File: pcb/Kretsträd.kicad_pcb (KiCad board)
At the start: 2 copper layers, 112.5 x 95.1 mm, 58 parts, among them J1 Conn_01x02_Female, J2 Conn_01x02_Female, J3 Conn_01x02_Female, SW1 SW_PUSH, SW10 SW_PUSH, SW11 SW_PUSH, SW12 SW_PUSH, SW13 SW_PUSH, SW14 SW_PUSH, SW15 SW_PUSH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

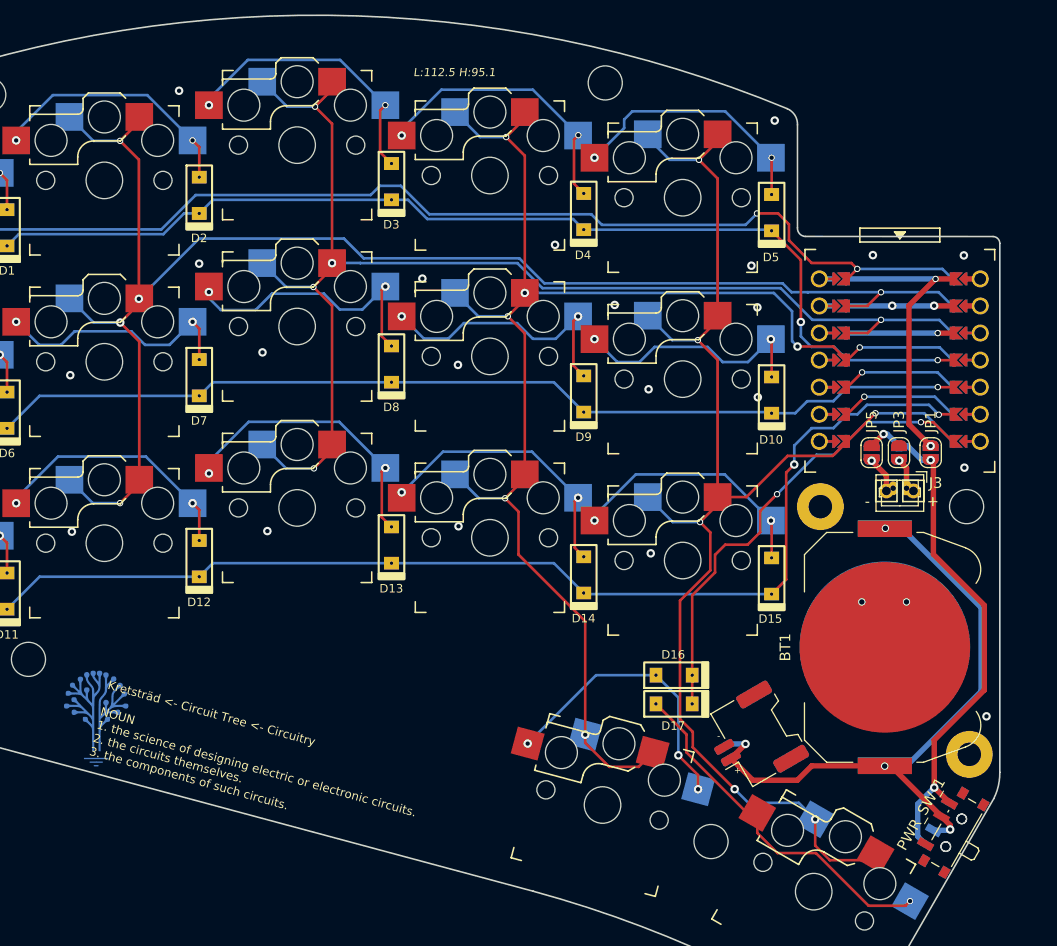
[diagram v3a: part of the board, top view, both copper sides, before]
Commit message: Moved position of CR2032 battery holder, some mounting holes.
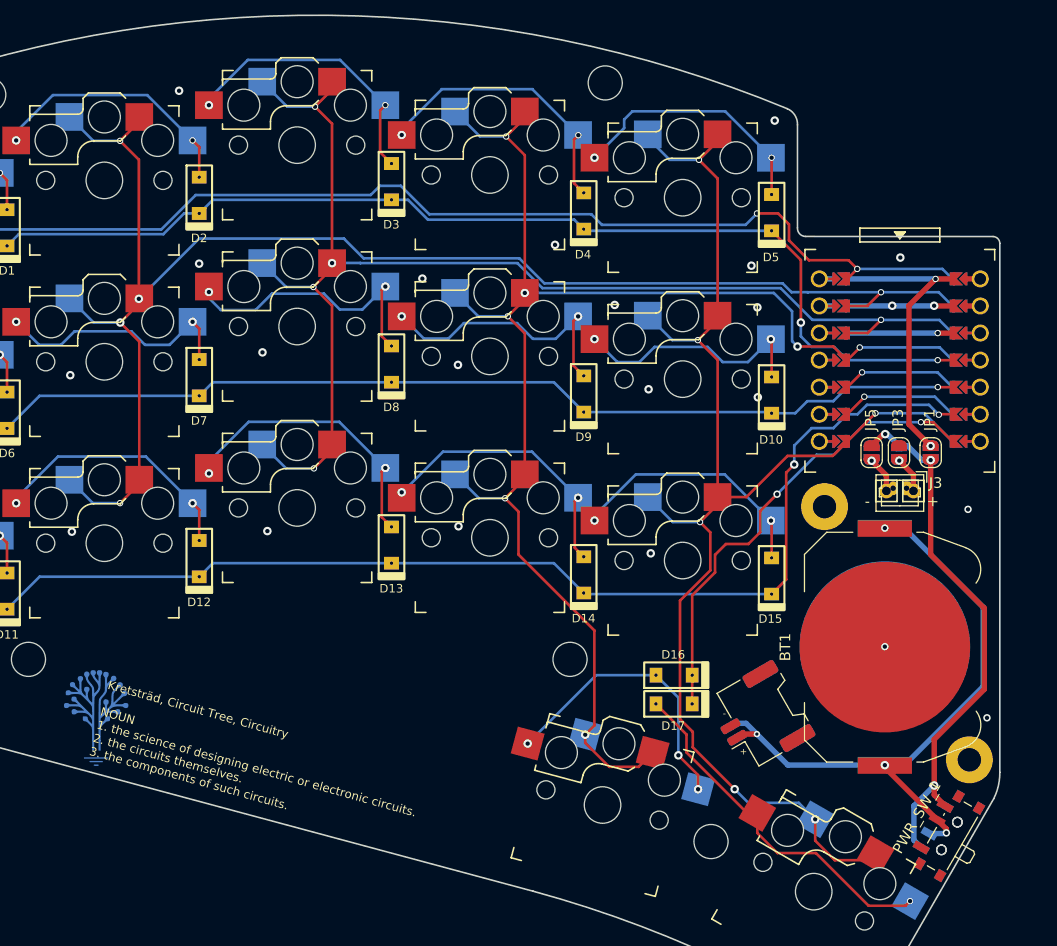
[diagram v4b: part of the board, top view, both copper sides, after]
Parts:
- moved TH5 39.9 mm to (154.6, 106.9)
- moved J1 2.02 mm to (172.4, 112.4)
- moved J2 2.02 mm to (172.4, 112.4)
- moved TH_PCB_2 0.51 mm to (192.0, 116.4)
- moved PWR_SW_1 0.51 mm to (189.9, 123.3)
- moved PWR_SW_2 0.51 mm to (189.9, 123.3)
- moved TH_PCB_1 0.39 mm to (178.4, 92.6)
- moved D4 0.05 mm to (155.9, 64.9)
- moved SW4 0.05 mm to (147.0, 61.5)
- moved G*** 0.05 mm to (109.9, 111.4)
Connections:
- SW1 pad : col0 -> (no net)
- SW11 pad : col0 -> (no net)
- SW6 pad : col0 -> (no net)
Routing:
- net BT+: track 62.4 -> 55.8 mm
- net col4: track 127.4 -> 126.4 mm
- net col3: track 134.7 -> 135.4 mm
- net row0: track 101.4 -> 100.7 mm
- net Net-(JP1-Pad1): track 50.1 -> 50.8 mm
- net Hole_1: track 2.87 -> 3.40 mm
- net GND: track 9.88 -> 9.87 mm, vias 26 -> 24
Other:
- board text added: "Kretsträd, Circuit Tree, Circuitry NOUN 1. the science of designing electric or electronic circuits. 2. the circuits themselves. 3. the components of such circuits."
- board text removed: "Kretsträd <- Circuit Tree <- Circuitry NOUN 1. the science of designing electric or electronic circuits. 2. the circuits themselves. 3. the components of such circuits."
- board text removed: "L:112.5 H:95.1"

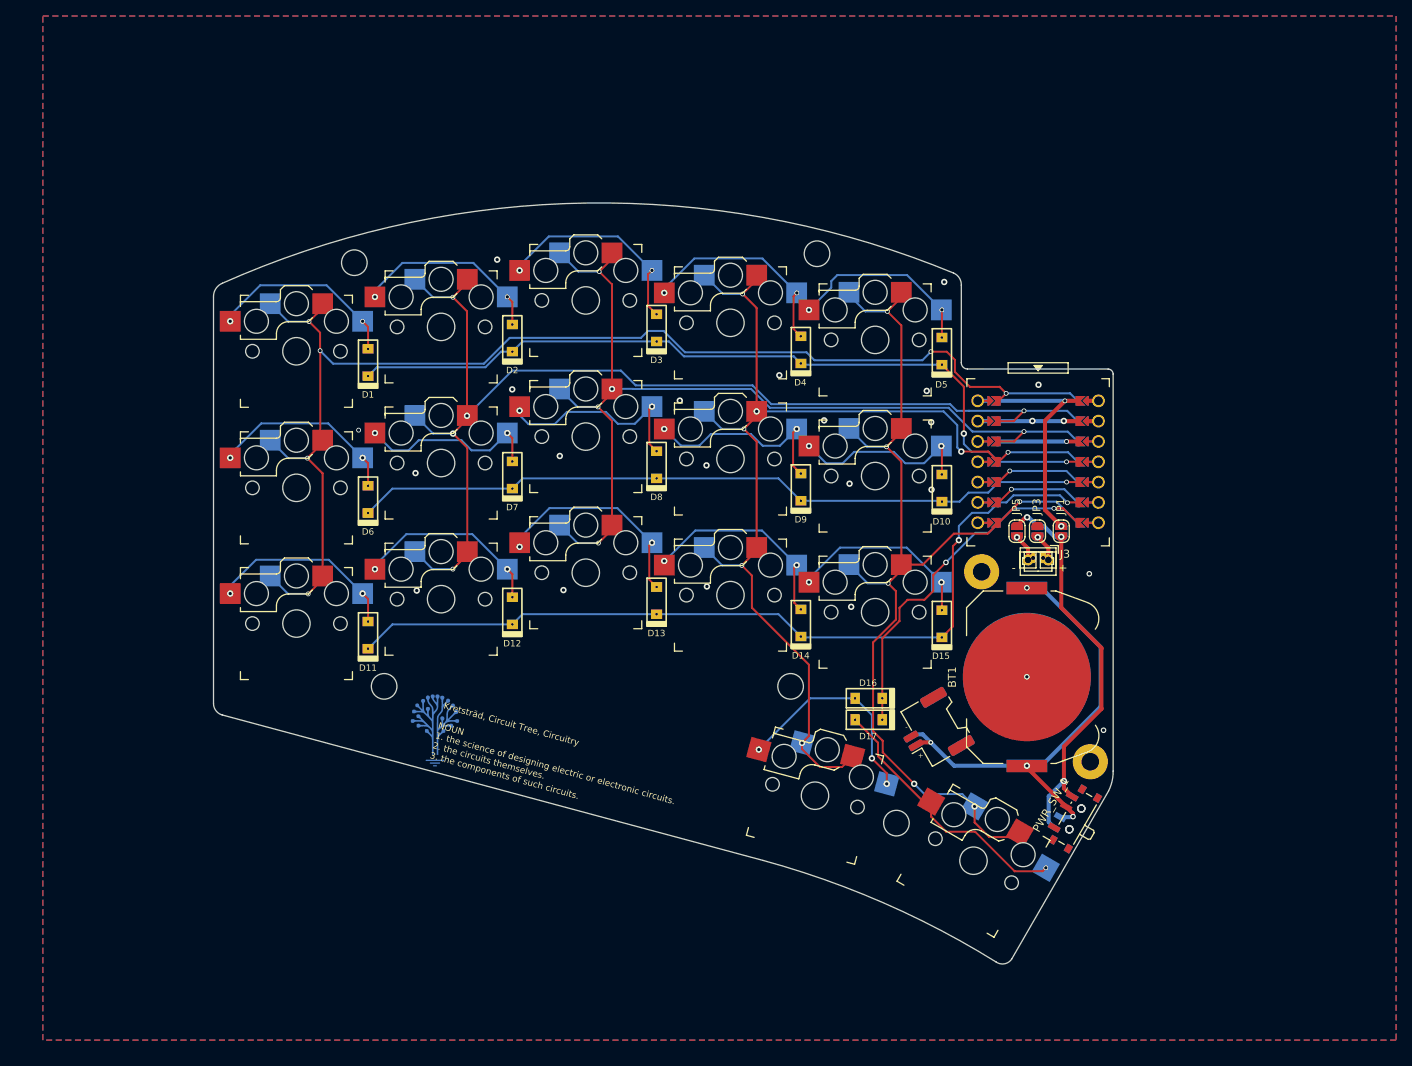
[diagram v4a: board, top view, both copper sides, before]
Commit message: 1. Corrected all vias' size. 2. Minor change to circuit tree logo and text. 3. Other changes for aesthetics reasons.
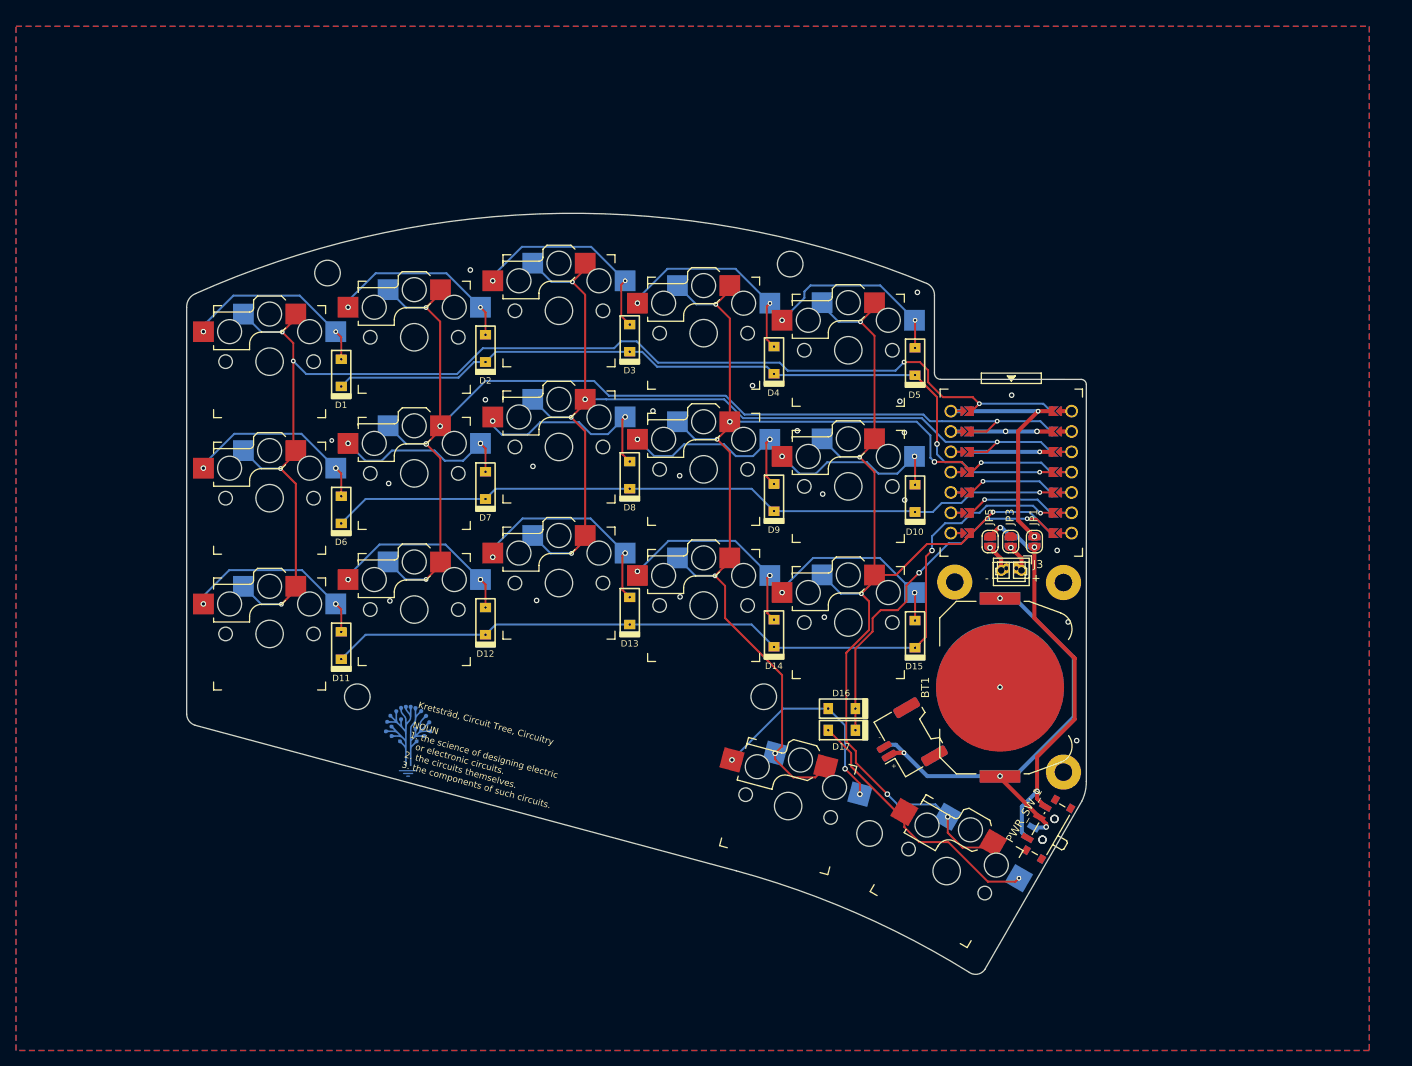
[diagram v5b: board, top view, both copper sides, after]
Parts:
- added TH_PCB_3: HOLE, MountingHole:MountingHole_2.2mm_M2_Pad, F.Cu at (188.7, 117.7)
- moved TH_PCB_2 22.7 mm to (188.7, 94.0)
- moved JP3 3.60 mm to (182.1, 88.8)
- moved JP4 3.60 mm to (182.1, 88.9)
- moved TH2 3.60 mm to (154.5, 54.2)
- moved BT1 3.60 mm to (180.7, 107.1)
- moved BT2 3.60 mm to (180.7, 107.0)
- moved D1 3.60 mm to (98.4, 67.7)
- moved D10 3.60 mm to (170.1, 83.4)
- moved D12 3.60 mm to (116.4, 98.8)
- moved D13 3.60 mm to (134.5, 97.5)
- moved D14 3.60 mm to (152.5, 100.3)
- moved D15 3.60 mm to (170.1, 100.4)
- moved D16 3.60 mm to (161.0, 109.7)
- moved D17 3.60 mm to (161.0, 112.4)
- moved D3 3.60 mm to (134.5, 63.4)
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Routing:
- net GND: vias 24 -> 25

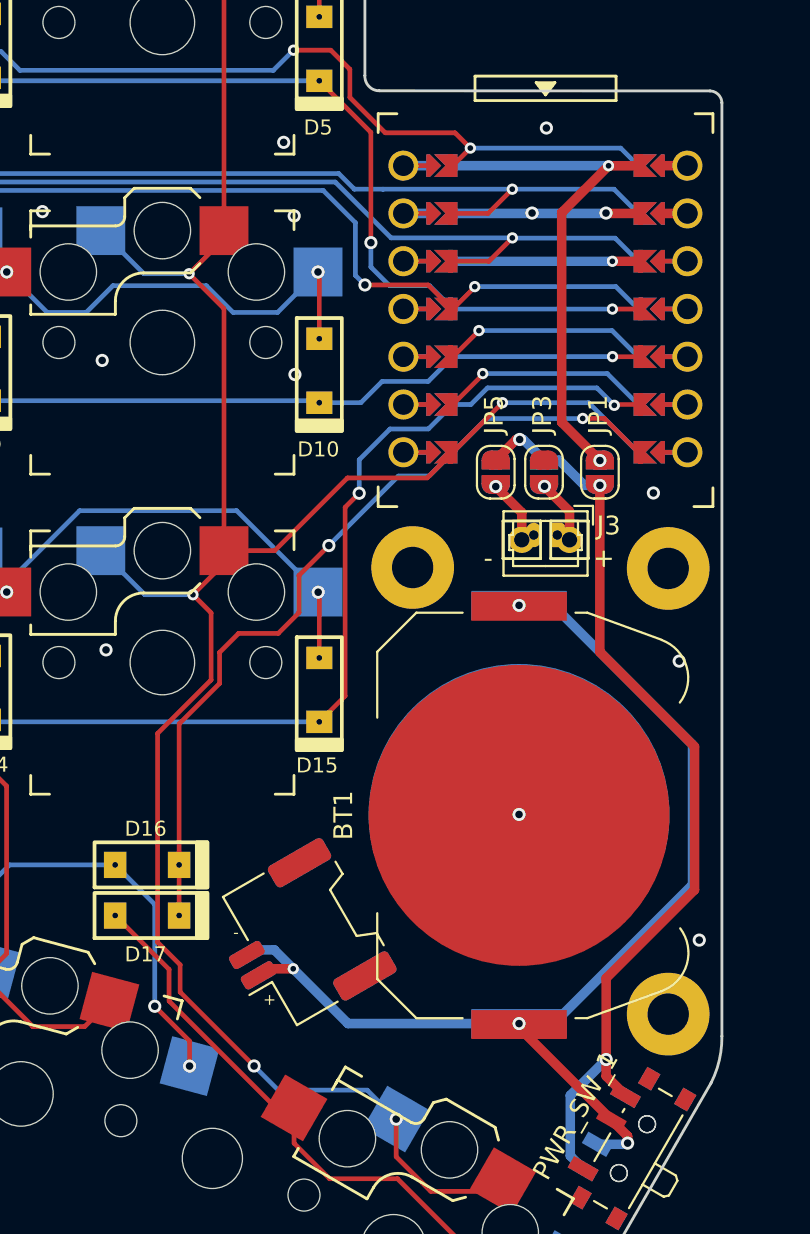
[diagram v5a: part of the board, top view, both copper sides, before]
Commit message: 1. Modified LIR2032 battery holder footprint. 2. Changed Molex 1.25 battery female connector location. 3. Minor changes.
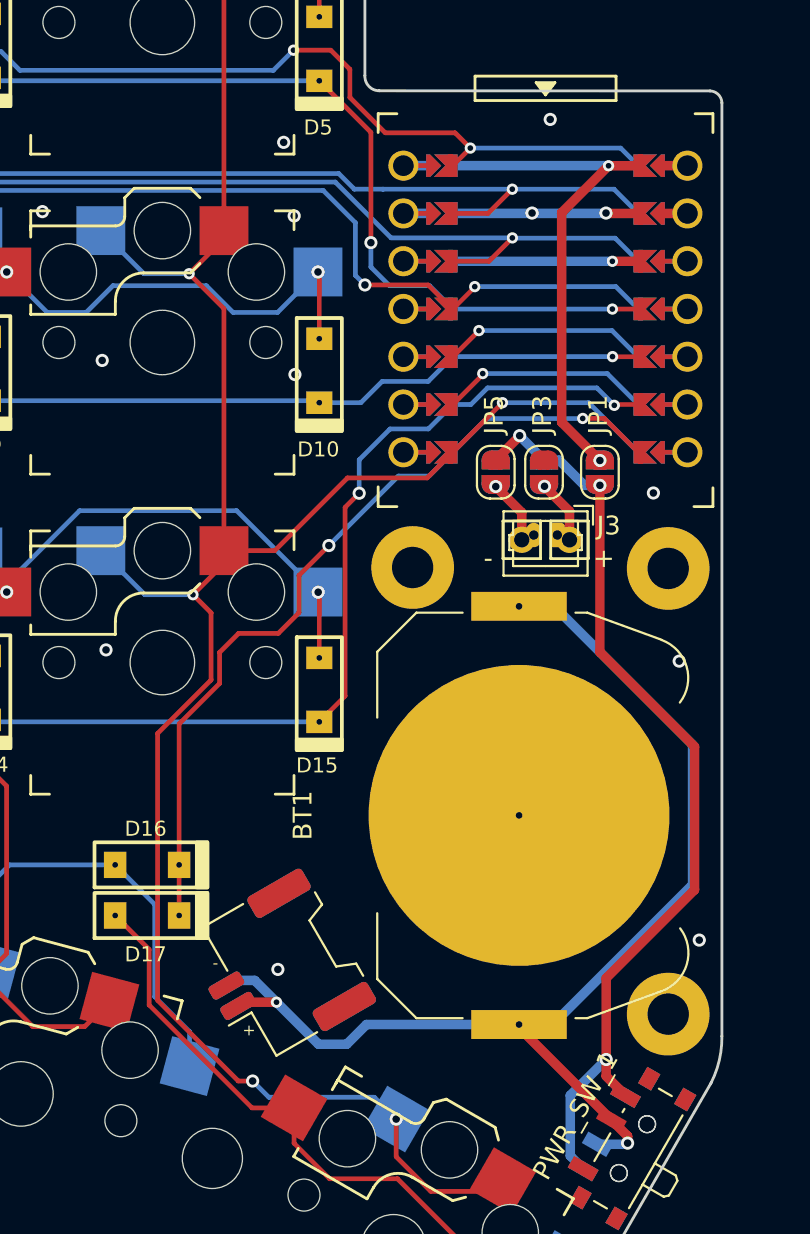
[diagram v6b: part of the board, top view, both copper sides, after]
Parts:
- removed BT2: Battery_Cell, jw_custom_footprint:BatteryHolder_Keystone_3034_1x20mm_mod
- BT1: footprint jw_custom_footprint:BatteryHolder_Keystone_3034_1x20mm_mod -> jw_custom_footprint:BatteryHolder_Keystone_3034_1x20mm_mod_dual_side
- moved J1 1.96 mm to (167.9, 115.3)
- moved J2 1.96 mm to (167.9, 115.3)
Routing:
- net Net-(D17-Pad2): track 32.8 -> 34.7 mm
- net BT+: track 55.8 -> 57.5 mm, vias 4 -> 2
- net col4: track 126.4 -> 127.4 mm
- net Net-(D16-Pad2): vias 3 -> 1
